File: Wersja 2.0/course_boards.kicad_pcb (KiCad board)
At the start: 2 copper layers, 160.7 x 83.8 mm, 38 parts, among them J1 POWER_SOCKET, Q1 BC547, Q3 BC547, SW1 SW_Push, SW2 SW_Push, SW3 SW_Push, U1 ESP32-C3-DevKitM-1

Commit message: fix ver 2
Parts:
- added ?: , , F.Cu at (204.0, 123.7)
- added ?: , , F.Cu at (166.6, 120.4)
- added ?: , , F.Cu at (171.2, 123.2)
- added ?: , , F.Cu at (169.7, 123.2)
- added ?: , , F.Cu at (198.9, 120.1)
- added ?: , , F.Cu at (186.2, 123.7)
- added ?: , , F.Cu at (193.8, 123.7)
- added ?: , , F.Cu at (188.7, 120.1)
- added ?: , , F.Cu at (174.2, 120.4)
- added ?: , , F.Cu at (177.3, 120.4)
- added ?: , , F.Cu at (171.2, 120.4)
- added ?: , , F.Cu at (169.7, 120.4)
- added ?: , , F.Cu at (172.7, 120.4)
- added ?: , , F.Cu at (168.1, 123.2)
- added ?: , , F.Cu at (175.8, 123.2)
- added ?: , , F.Cu at (196.3, 123.7)
- added ?: , , F.Cu at (174.2, 123.2)
- added ?: , , F.Cu at (196.3, 120.1)
- added ?: , , F.Cu at (201.4, 120.1)
- added ?: , , F.Cu at (172.7, 123.2)
- added ?: , , F.Cu at (198.9, 123.7)
- added ?: , , F.Cu at (166.6, 123.2)
- added ?: , , F.Cu at (191.3, 120.1)
- added ?: , , F.Cu at (186.2, 120.1)
- added ?: , , F.Cu at (175.8, 120.4)
- added ?: , , F.Cu at (191.3, 123.7)
- added ?: , , F.Cu at (204.0, 120.1)
- added ?: , , F.Cu at (201.4, 123.7)
- added ?: , , F.Cu at (188.7, 123.7)
- added ?: , , F.Cu at (177.3, 123.2)
- added ?: , , F.Cu at (168.1, 120.4)
- added ?: , , F.Cu at (193.8, 120.1)
- added J2: I2C_CONN, Connector_PinHeader_2.54mm:PinHeader_1x04_P2.54mm_Vertical, F.Cu at (203.2, 109.0)
- added J4: UART_CONN, Connector_PinHeader_2.54mm:PinHeader_1x04_P2.54mm_Vertical, F.Cu at (190.3, 109.2)
- U1: value ESP32-C3-DevKitM-1 -> ESP32-C6-DevKitC-1; footprint RF_Module:ESP32-C3-DevKitM-1 -> PCM_Espressif:ESP32-C6-DevKitC-1
- moved RV5K1 50.8 mm to (190.1, 65.2), turned to 180 degrees
- moved U1 48.1 mm to (180.5, 97.5), turned to 180 degrees
- moved D10 10.1 mm to (200.0, 91.0)
- moved D3 10.1 mm to (189.8, 91.0)
- moved R4 6.28 mm to (189.8, 76.4)
- moved R7 6.28 mm to (200.0, 76.4)
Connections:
- R4 pad 1: Net-(U1-IO4) -> Net-(U1-GPIO2)
- R7 pad 1: Net-(U1-IO5) -> Net-(U1-GPIO3)
- RV5K1 pad 1: VCC -> 3V3
- RV5K1 pad 2: Net-(U1-IO0) -> Net-(U1-GPIO4/MTMS)
- U1 pad 1: GND -> 3V3
- U1 pad 10: Net-(J2-Pin_2) (its old number) -> unconnected-(U1-GPIO10-Pad10)
- U1 pad 12: GND -> Net-(U1-GPIO2)
- U1 pad 13: Net-(U1-5V-Pad13) -> Net-(U1-GPIO3)
- U1 pad 14: Net-(U1-5V-Pad13) -> VCC
- U1 pad 16: GND -> unconnected-(U1-NC-Pad16)
- U1 pad 18: unconnected-(U1-IO18-Pad18) -> GND
- U1 pad 19: GND -> unconnected-(U1-GPIO12/USB_D--Pad19)
- U1 pad 2: VCC -> unconnected-(U1-EN/RESET-Pad2)
- U1 pad 20: Net-(U1-IO4) -> unconnected-(U1-GPIO13/USB_D+-Pad20)
- U1 pad 21: Net-(U1-IO5) -> GND
- U1 pad 24: GND -> unconnected-(U1-GPIO19-Pad24)
- U1 pad 27: GND -> unconnected-(U1-GPIO22-Pad27)
- U1 pad 28: Net-(J3-Pin_2) -> unconnected-(U1-GPIO23-Pad28)
- U1 pad 29: Net-(J3-Pin_1) -> unconnected-(U1-GPIO15/JTAG-Pad29)
- U1 pad 3: VCC -> Net-(U1-GPIO4/MTMS)
- U1 pad 30: GND -> unconnected-(U1-GPIO17/U0RXD-Pad30)
- U1 pad 5: unconnected-(U1-IO3-Pad5) -> Net-(J2-Pin_3)
- U1 pad 6: GND -> unconnected-(U1-GPIO7-Pad6)
- U1 pad 7: unconnected-(U1-RST-Pad7) -> Net-(J4-Pin_3)
- U1 pad 8: GND -> Net-(J4-Pin_2)
- U1 pad 9: Net-(U1-IO0) -> unconnected-(U1-GPIO8/BOOT-Pad9)
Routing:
- net 3V3: track 0.00 -> 61.1 mm
- net Net-(U1-IO0): track 43.0 -> 0.00 mm
- net Net-(J4-Pin_2): track 0.00 -> 40.9 mm
- net Net-(U1-GPIO4/MTMS): track 0.00 -> 36.4 mm
- net Net-(J4-Pin_3): track 0.00 -> 33.3 mm
- net Net-(J2-Pin_2): track 0.00 -> 29.5 mm
- net Net-(J2-Pin_3): track 0.00 -> 29.5 mm
- net Net-(U1-GPIO3): track 0.00 -> 23.3 mm
- net GND: track 477.2 -> 499.2 mm
- net Net-(U1-IO5): track 18.2 -> 0.00 mm
- net Net-(U1-GPIO2): track 0.00 -> 12.1 mm
- net Net-(U1-IO4): track 7.03 -> 0.00 mm
- net Net-(D3-A): track 8.25 -> 4.43 mm
- net Net-(D10-A): track 8.25 -> 4.43 mm
- net VCC: track 329.9 -> 328.6 mm
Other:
- board size 160.7 x 83.8 mm -> 164.3 x 83.8 mm
- board text added: "3V3"
- board text added: "Pady do nauki:"
- board text added: "RX"
- board text added: "SCK"
- board text added: "SDA"
- board text added: "TX"

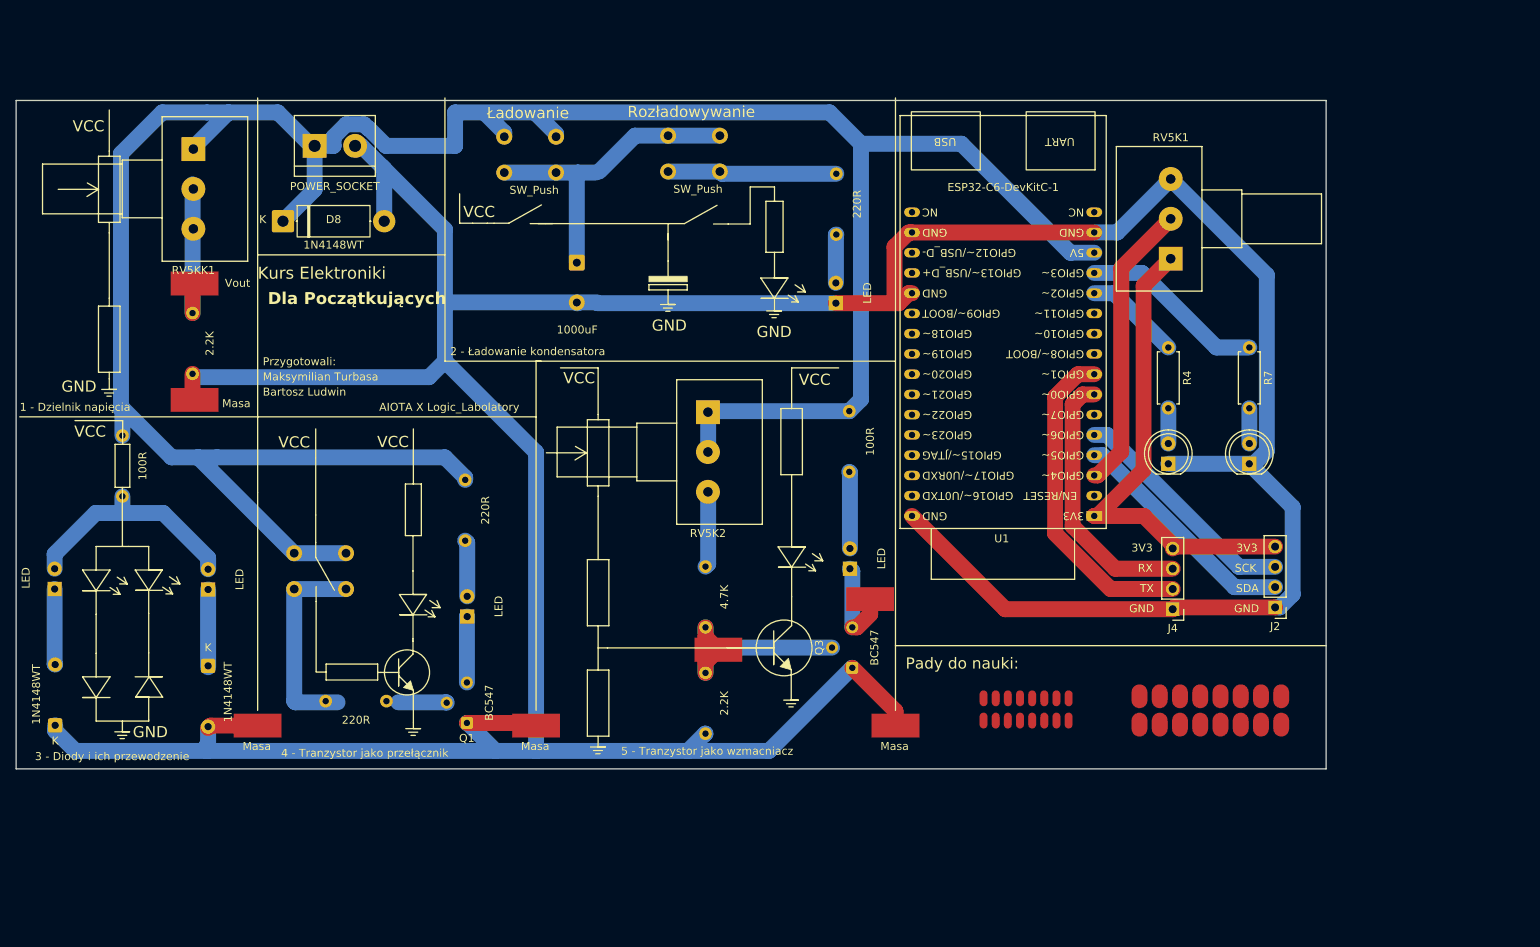
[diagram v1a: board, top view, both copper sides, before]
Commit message: add more space in esp section
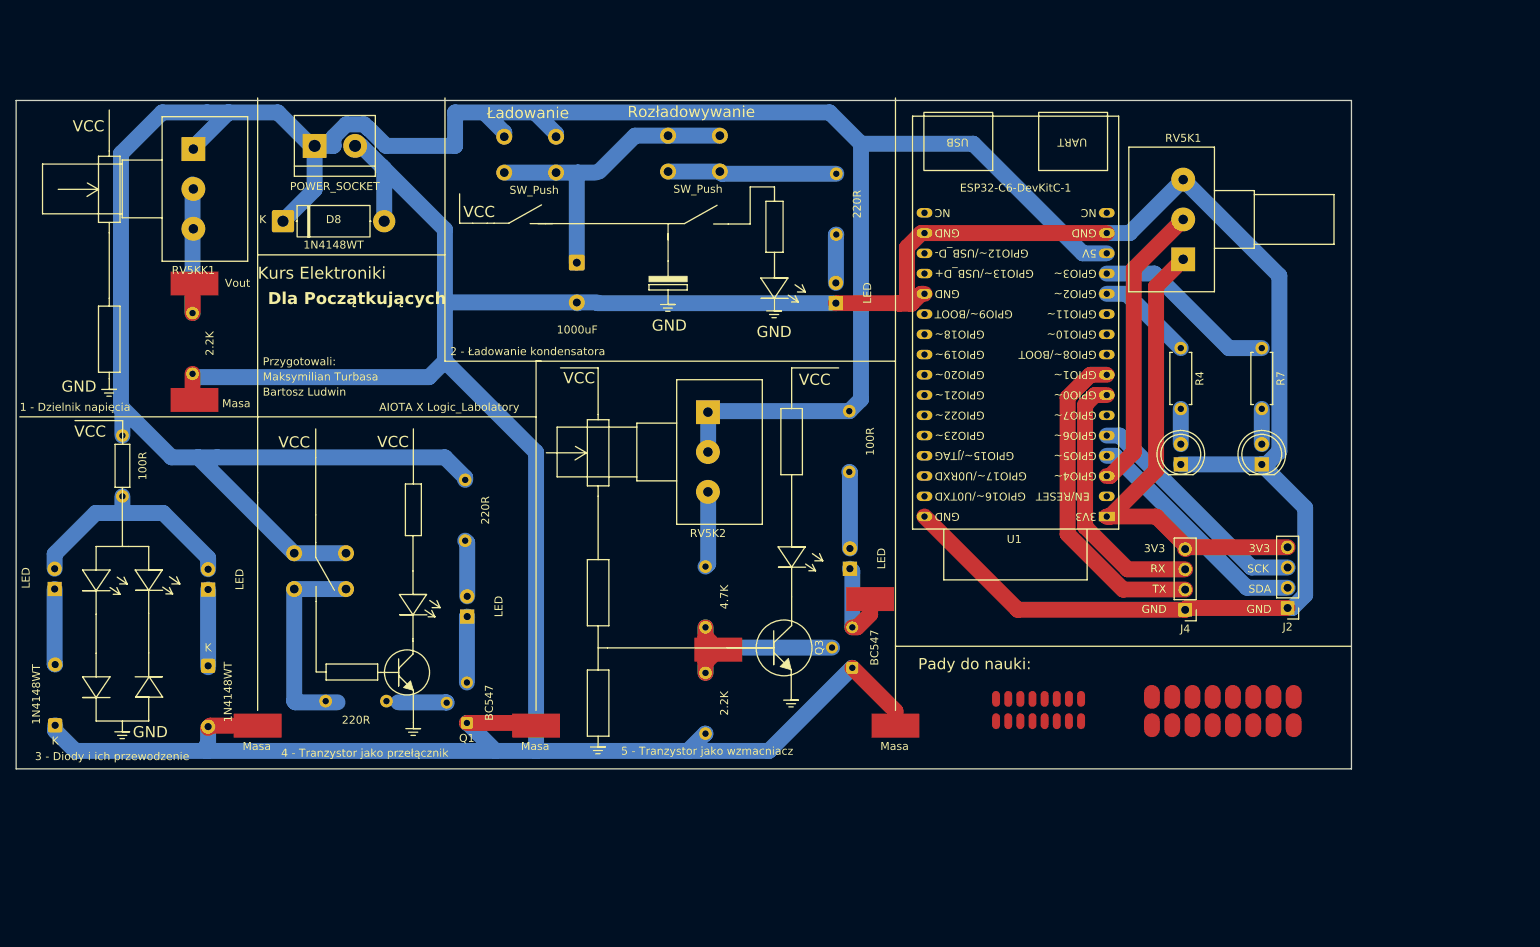
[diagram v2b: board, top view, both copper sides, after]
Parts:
- moved ? 1.57 mm to (205.5, 123.8)
- moved ? 1.57 mm to (168.2, 120.5)
- moved ? 1.57 mm to (172.8, 123.3)
- moved ? 1.57 mm to (171.2, 123.3)
- moved ? 1.57 mm to (200.4, 120.2)
- moved ? 1.57 mm to (187.7, 123.8)
- moved ? 1.57 mm to (195.4, 123.8)
- moved ? 1.57 mm to (190.3, 120.2)
- moved ? 1.57 mm to (175.8, 120.5)
- moved ? 1.57 mm to (178.9, 120.5)
- moved ? 1.57 mm to (172.8, 120.5)
- moved ? 1.57 mm to (171.2, 120.5)
- moved ? 1.57 mm to (174.3, 120.5)
- moved ? 1.57 mm to (169.7, 123.3)
- moved ? 1.57 mm to (177.3, 123.3)
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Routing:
- net GND: track 499.2 -> 500.8 mm
- net VCC: track 328.6 -> 330.2 mm
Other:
- board size 164.3 x 83.8 mm -> 167.5 x 83.8 mm

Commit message: add drone logo
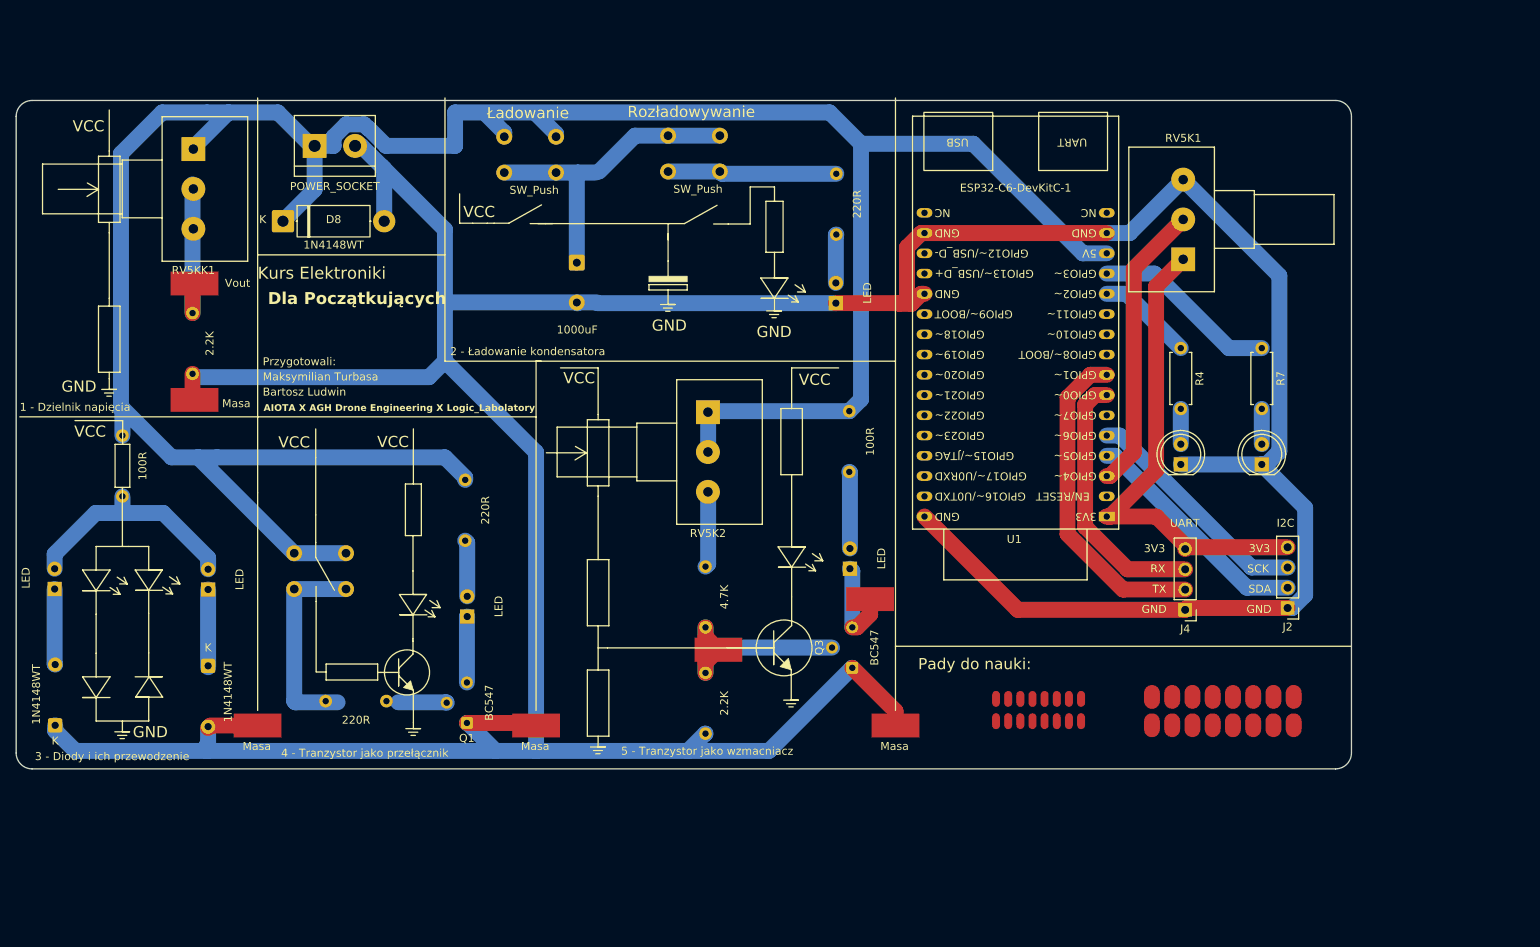
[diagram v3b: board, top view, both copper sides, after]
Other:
- outline, holes or cut-outs redrawn
- board text added: "AIOTA X AGH Drone Engineering X Logic_Labolatory"
- board text added: "I2C"
- board text added: "UART"
- board text removed: "AIOTA X Logic_Labolatory"
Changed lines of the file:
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@@
 		(layer "F.SilkS")
 	)
-	(gr_rect
-		(start 45.27 45.4025)
-		(end 212.775 129.25)
-		(stroke
-			(width 0.05)
-			(type default)
-		)
-		(fill no)
+	(gr_arc
+		(start 210.775 45.4025)
+		(mid 212.189214 45.988286)
+		(end 212.775 47.4025)
+		(stroke
+			(width 0.05)
+			(type default)
+		)
+		(layer "Edge.Cuts")
+	)
+	(gr_line
+		(start 45.27 127.25)
+		(end 45.27 47.4025)
+		(stroke
+			(width 0.05)
+			(type default)
+		)
+		(layer "Edge.Cuts")
+	)
+	(gr_arc
+		(start 212.775 127.25)
+		(mid 212.189214 128.664214)
+		(end 210.775 129.25)
+		(stroke
+			(width 0.05)
+			(type default)
+		)
+		(layer "Edge.Cuts")
+	)
+	(gr_arc
+		(start 45.27 47.4025)
+		(mid 45.855786 45.988286)
+		(end 47.27 45.4025)
+		(stroke
+			(width 0.05)
+			(type default)
+		)
+		(layer "Edge.Cuts")
+	)
+	(gr_line
+		(start 47.27 45.4025)
+		(end 210.775 45.4025)
+		(stroke
+			(width 0.05)
+			(type default)
+		)
+		(layer "Edge.Cuts")
+	)
+	(gr_line
+		(start 210.775 129.25)
+		(end 47.27 129.25)
+		(stroke
+			(width 0.05)
+			(type default)
+		)
+		(layer "Edge.Cuts")
+	)
+	(gr_line
+		(start 212.775 47.4025)
+		(end 212.775 127.25)
+		(stroke
+			(width 0.05)
+			(type default)
+		)
+		(layer "Edge.Cuts")
+	)
+	(gr_arc
+		(start 47.27 129.25)
+		(mid 45.855786 128.664214)
+		(end 45.27 127.25)
+		(stroke
+			(width 0.05)
+			(type default)
+		)
 		(layer "Edge.Cuts")
 	)
@@
 		)
 	)
+	(gr_text "I2C"
+		(at 203.386 99 0)
+		(layer "F.SilkS")
+		(effects
+			(font
+				(size 1 1)
+				(thickness 0.1)
+			)
+			(justify left bottom)
+		)
+	)
 	(gr_text "RX"
 		(at 187.541524 104.724684 0)
@@
 		)
 	)
-	(gr_text "AIOTA X Logic_Labolatory"
-		(at 90.805 84.455 0)
-		(layer "F.SilkS")
-		(effects
-			(font
-				(size 1 1)
-				(thickness 0.1)
+	(gr_text "AIOTA X AGH Drone Engineering X Logic_Labolatory"
+		(at 76.3 84.455 0)
+		(layer "F.SilkS")
+		(effects
+			(font
+				(size 0.85 0.85)
+				(thickness 0.15)
+				(bold yes)
 			)
 			(justify left bottom)
@@
 				(thickness 0.1)
 			)
+			(justify left bottom)
+		)
+	)
+	(gr_text "UART"
+		(at 190 99 0)
+		(layer "F.SilkS")
+		(effects
+			(font
+				(size 1 1)
+				(thickness 0.1)
+			)
